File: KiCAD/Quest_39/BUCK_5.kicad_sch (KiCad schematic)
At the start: 21 parts

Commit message: Fixed most ERC errors
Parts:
- gave numbers to parts that had none: 21
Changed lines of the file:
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@@
   (symbol (lib_id "Device:R") (at 60.96 49.53 0) (unit 1)
     (in_bom yes) (on_board yes) (fields_autoplaced)
-    (property "Reference" "R?" (id 0) (at 63.5 48.2599 0)
+    (property "Reference" "R35" (id 0) (at 63.5 48.2599 0)
       (effects (font (size 1.27 1.27)) (justify left))
     )
@@
   (symbol (lib_id "Device:R") (at 48.26 49.53 0) (unit 1)
     (in_bom yes) (on_board yes) (fields_autoplaced)
-    (property "Reference" "R?" (id 0) (at 50.8 48.2599 0)
+    (property "Reference" "R34" (id 0) (at 50.8 48.2599 0)
       (effects (font (size 1.27 1.27)) (justify left))
     )
@@
   (symbol (lib_id "Device:C_Polarized") (at 381 172.72 0) (unit 1)
     (in_bom yes) (on_board yes)
-    (property "Reference" "C?" (id 0) (at 384.7895 171.4075 0)
+    (property "Reference" "C86" (id 0) (at 384.7895 171.4075 0)
       (effects (font (size 1.27 1.27)) (justify left))
     )
@@
   (symbol (lib_id "Device:C_Polarized") (at 393.7 172.72 0) (unit 1)
     (in_bom yes) (on_board yes)
-    (property "Reference" "C?" (id 0) (at 397.4895 171.4075 0)
+    (property "Reference" "C87" (id 0) (at 397.4895 171.4075 0)
       (effects (font (size 1.27 1.27)) (justify left))
     )
@@
   (symbol (lib_id "Device:C_Polarized") (at 86.36 46.99 0) (unit 1)
     (in_bom yes) (on_board yes) (fields_autoplaced)
-    (property "Reference" "C?" (id 0) (at 90.17 44.8309 0)
+    (property "Reference" "C77" (id 0) (at 90.17 44.8309 0)
       (effects (font (size 1.27 1.27)) (justify left))
     )
@@
   (symbol (lib_id "Device:C") (at 125.73 46.99 0) (unit 1)
     (in_bom yes) (on_board yes) (fields_autoplaced)
-    (property "Reference" "C?" (id 0) (at 129.54 45.7199 0)
+    (property "Reference" "C80" (id 0) (at 129.54 45.7199 0)
       (effects (font (size 1.27 1.27)) (justify left))
     )
@@
   (symbol (lib_id "Analog_ADC:INA226") (at 78.74 73.66 0) (unit 1)
     (in_bom yes) (on_board yes)
-    (property "Reference" "U?" (id 0) (at 83.82 62.23 0)
+    (property "Reference" "U25" (id 0) (at 83.82 62.23 0)
       (effects (font (size 1.27 1.27)) (justify left))
     )
@@
   (symbol (lib_id "Device:R") (at 322.58 215.9 0) (unit 1)
     (in_bom yes) (on_board yes) (fields_autoplaced)
-    (property "Reference" "R?" (id 0) (at 325.12 214.6299 0)
+    (property "Reference" "R37" (id 0) (at 325.12 214.6299 0)
       (effects (font (size 1.27 1.27)) (justify left))
     )
@@
   (symbol (lib_id "Device:C") (at 100.33 46.99 0) (unit 1)
     (in_bom yes) (on_board yes) (fields_autoplaced)
-    (property "Reference" "C?" (id 0) (at 104.14 45.7199 0)
+    (property "Reference" "C78" (id 0) (at 104.14 45.7199 0)
       (effects (font (size 1.27 1.27)) (justify left))
     )
@@
   (symbol (lib_id "Amplifier_Operational:MCP601-xOT") (at 35.56 66.04 0) (unit 1)
     (in_bom yes) (on_board yes)
-    (property "Reference" "U?" (id 0) (at 38.1 62.23 0))
+    (property "Reference" "U24" (id 0) (at 38.1 62.23 0))
     (property "Value" "MCP601T-I/OT" (id 1) (at 41.91 69.85 0))
     (property "Footprint" "Package_TO_SOT_SMD:SOT-23-5" (id 2) (at 33.02 71.12 0)
@@
   (symbol (lib_id "MCP4151:MCP4151-502E{slash}SN") (at 254 220.98 0) (unit 1)
     (in_bom yes) (on_board yes)
-    (property "Reference" "U?" (id 0) (at 312.42 214.63 0)
+    (property "Reference" "U27" (id 0) (at 312.42 214.63 0)
       (effects (font (size 1.524 1.524)))
     )
@@
   (symbol (lib_id "Device:C") (at 128.27 137.16 0) (unit 1)
     (in_bom yes) (on_board yes) (fields_autoplaced)
-    (property "Reference" "C?" (id 0) (at 132.08 135.8899 0)
+    (property "Reference" "C82" (id 0) (at 132.08 135.8899 0)
       (effects (font (size 1.27 1.27)) (justify left))
     )
@@
   (symbol (lib_id "Device:C") (at 335.28 172.72 0) (unit 1)
     (in_bom yes) (on_board yes) (fields_autoplaced)
-    (property "Reference" "C?" (id 0) (at 339.09 171.4499 0)
+    (property "Reference" "C83" (id 0) (at 339.09 171.4499 0)
       (effects (font (size 1.27 1.27)) (justify left))
     )
@@
   (symbol (lib_id "LTM4611EV:LTM4611EV-PBF") (at 132.08 102.87 0) (unit 1)
     (in_bom yes) (on_board yes)
-    (property "Reference" "U?" (id 0) (at 308.61 50.8 0)
+    (property "Reference" "U26" (id 0) (at 308.61 50.8 0)
       (effects (font (size 1.524 1.524)))
     )
@@
   (symbol (lib_id "Device:C_Polarized") (at 368.3 172.72 0) (unit 1)
     (in_bom yes) (on_board yes)
-    (property "Reference" "C?" (id 0) (at 372.0895 171.4075 0)
+    (property "Reference" "C85" (id 0) (at 372.0895 171.4075 0)
       (effects (font (size 1.27 1.27)) (justify left))
     )
@@
   (symbol (lib_id "Device:R") (at 127 91.44 0) (unit 1)
     (in_bom yes) (on_board yes) (fields_autoplaced)
-    (property "Reference" "R?" (id 0) (at 129.54 90.1699 0)
+    (property "Reference" "R36" (id 0) (at 129.54 90.1699 0)
       (effects (font (size 1.27 1.27)) (justify left))
     )
@@
   (symbol (lib_id "Device:R") (at 55.88 41.91 90) (unit 1)
     (in_bom yes) (on_board yes) (fields_autoplaced)
-    (property "Reference" "R?" (id 0) (at 55.88 35.56 90))
+    (property "Reference" "R33" (id 0) (at 55.88 35.56 90))
     (property "Value" "0R0025" (id 1) (at 55.88 38.1 90))
     (property "Footprint" "" (id 2) (at 55.88 43.688 90)
@@
   (symbol (lib_id "Device:C") (at 55.88 55.88 90) (unit 1)
     (in_bom yes) (on_board yes)
-    (property "Reference" "C?" (id 0) (at 55.88 52.07 90))
+    (property "Reference" "C81" (id 0) (at 55.88 52.07 90))
     (property "Value" "1uF" (id 1) (at 55.88 59.69 90))
     (property "Footprint" "OptoDevice:R_LDR_4.9x4.2mm_P2.54mm_Vertical" (id 2) (at 59.69 54.9148 0)
@@
   (symbol (lib_id "Device:C") (at 113.03 46.99 0) (unit 1)
     (in_bom yes) (on_board yes) (fields_autoplaced)
-    (property "Reference" "C?" (id 0) (at 116.84 45.7199 0)
+    (property "Reference" "C79" (id 0) (at 116.84 45.7199 0)
       (effects (font (size 1.27 1.27)) (justify left))
     )
@@
   (symbol (lib_id "Device:C_Polarized") (at 354.33 172.72 0) (unit 1)
     (in_bom yes) (on_board yes)
-    (property "Reference" "C?" (id 0) (at 358.1195 171.4075 0)
+    (property "Reference" "C84" (id 0) (at 358.1195 171.4075 0)
       (effects (font (size 1.27 1.27)) (justify left))
     )
@@
   (symbol (lib_id "Device:C") (at 337.82 224.79 0) (unit 1)
     (in_bom yes) (on_board yes) (fields_autoplaced)
-    (property "Reference" "C?" (id 0) (at 341.63 223.5199 0)
-      (effects (font (size 1.27 1.27)) (justify left))
-    )
+    (property "Reference" "C88" (id 0) (at 341.63 223.5199 0)
+      (effects (font (size 1.27 1.27)) (justify left))
+    )

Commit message: Gave all INA226's unique addresses
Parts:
- removed C77: 330uF, symbol Device:C_Polarized
- removed C78, C79, C80: 22uF, symbol Device:C
- removed C81: 1uF, OptoDevice:R_LDR_4.9x4.2mm_P2.54mm_Vertical, symbol Device:C
- removed C82: 100nF, symbol Device:C
- removed C83: 100pF, symbol Device:C
- removed C85, C86, C87: 100uF, symbol Device:C_Polarized
- removed R33: 0R0025, symbol Device:R
- removed R34, R35: 10, symbol Device:R
- removed R36: 10K, symbol Device:R
- removed R37: 20K, symbol Device:R
- removed U24: MCP601T-I/OT, Package_TO_SOT_SMD:SOT-23-5, symbol Amplifier_Operational:MCP601-xOT
- added C85, C86, C87: 22uF, symbol Device:C
- added C89, C90, C97: 100nF, symbol Device:C
- added C91: 10nF, symbol Device:C
- added C92, C93, C94, C95: 100uF, symbol Device:C_Polarized
- added C96: 100pF, symbol Device:C
- added R52: 0R0025, symbol Device:R
- added R53, R54: 10R, symbol Device:R
- added R55: 9k, symbol Device:R
- added R56: 1k, symbol Device:R
- added R57: 10k, symbol Device:R
- added R58: 20K, symbol Device:R
- added TP41, TP42, TP43, TP44, TP45, TP46, TP47: TestPoint, symbol Connector:TestPoint
- added U24: AD626ANZ, N_8_ADI, symbol AD626ANZ:AD626ANZ
- C84: value 100uF -> 330uF
- C88: value 100nF -> 1uF; footprint (none) -> OptoDevice:R_LDR_4.9x4.2mm_P2.54mm_Vertical
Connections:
- net +5V: now also U25.1 (A1), U25.2 (A0), C90.1, C97.1, U24.6 (+VS); no longer C88.1
- net GND: now also C89.2, C90.2, C97.2, U24.2 (AGND), U24.3 (-VS); no longer C88.2, U25.1 (A1), U25.2 (A0), U25.3 (~{Alert})
- net NEG: now also C85.2, C86.2, C87.2, C91.1, C92.2, C93.2, C94.2, C95.2, R56.2, U24.1 (-IN); no longer U25.8 (Vbus)
- net P0A: now also R58.2
- net POS: now also C92.1, C93.1, C94.1, C95.1, C96.1; no longer C84.1
- net PV_POS: now also C84.1, U26.A1 (VIN), U26.A2 (VIN), U26.A3 (VIN), U26.A4 (VIN), U26.A5 (VIN), U26.A6 (VIN), U26.B1 (VIN), U26.B2 (VIN), U26.B3 (VIN), U26.B4 (VIN), U26.B5 (VIN), U26.B6 (VIN), U26.C1 (VIN), U26.C2 (VIN), U26.C3 (VIN), U26.C4 (VIN), U26.C5 (VIN), U26.C6 (VIN), C85.1, C86.1, C87.1, R52.1, R52.2, R53.1, R54.1, R55.1, R57.1
- net RUN: now also R57.2
- net TRACK/SS: now also C91.2
- net Vfb: now also C96.2, R58.1
- net Vin+: now also C88.1, R53.2
- net Vin-: now also C88.2, U25.8 (Vbus), U25.9 (Vin-), R54.2, TP42.1, U24.5 (OUT)
- net at U26.A11 (COMP): now also TP45.1
- net at U26.A7 (INTVCC): now also U26.D9 (INTVCC), TP41.1
- net at U26.B12 (PLLFLTR/FSET): now also TP44.1
- net at U26.F11 (PGOOD): now also U26.G12 (PGOOD), TP43.1
- net at U26.K12 (DIFFVOUT), U26.L12 (VOUT_LCL): now also TP46.1, TP47.1
- new net: C89.1, U24.4 (FILTER)
- new net +IN: R55.2, R56.1, U24.8 (+IN)
- no-connect marks 16 -> 12
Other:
- note added: "10:1 divider"
- note added: "Addr=0x45"
- note added: "Extra mounting"
- note added: "G=10"
- note added: "Output voltage is set by varying Rfb with a digipot. SPI = 00"
- note added: "the measured voltage is divided and then amplified by 10 as to simulate a follower. This is done to make use of the AD626 (low price and availability)."

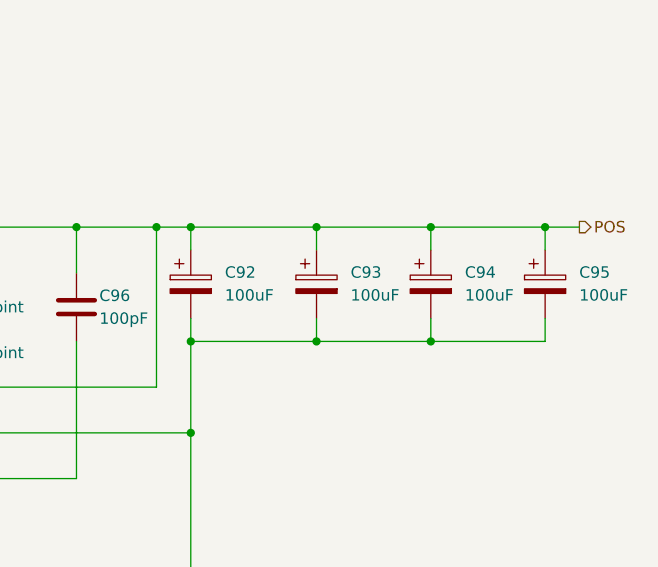
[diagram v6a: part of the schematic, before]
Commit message: Assigned all schem. symbols their footprints
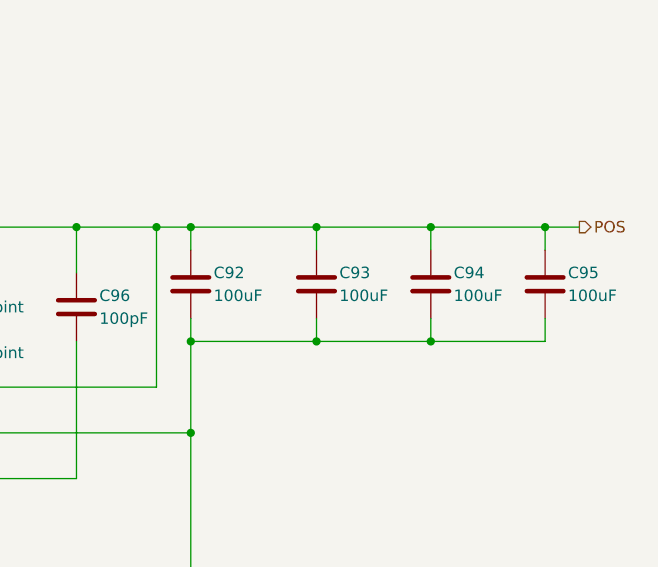
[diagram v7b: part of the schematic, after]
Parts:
- removed C92, C93, C94, C95: 100uF, symbol Device:C_Polarized
- added C92, C93, C94, C95: 100uF, Capacitor_SMD:C_1206_3216Metric, symbol Device:C
- C84: footprint (none) -> Capacitor_SMD:CP_Elec_8x6.9
- C85, C86, C87, C89, C90, C91, C96, C97: footprint (none) -> Capacitor_SMD:C_0805_2012Metric
- C88: footprint OptoDevice:R_LDR_4.9x4.2mm_P2.54mm_Vertical -> Capacitor_SMD:C_0805_2012Metric
- R52: footprint (none) -> Resistor_SMD:R_1206_3216Metric
- R53, R54, R55, R56, R57, R58: footprint (none) -> Resistor_SMD:R_0805_2012Metric
- TP41, TP42, TP43, TP44, TP45, TP46, TP47: footprint (none) -> TestPoint:TestPoint_Pad_D2.0mm
- U24: footprint N_8_ADI -> Package_DIP:DIP-8_W7.62mm_Socket_LongPads
- U26: footprint LGA-133_3_LIT -> Package_LGA:Linear_LGA-133_15.0x15.0mm_Layout12x12_P1.27mm
- U27: footprint SOIC8-N_MC_MCH -> Package_SO:MSOP-8_3x3mm_P0.65mm
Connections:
- net NEG: now also C92.2, C93.2, C94.2, C95.2
- net POS: now also C92.1, C93.1, C94.1, C95.1

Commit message: Initial work on layout
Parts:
- C88, C89, C90, C91, C96, C97: footprint Capacitor_SMD:C_0805_2012Metric -> Capacitor_SMD:C_0603_1608Metric
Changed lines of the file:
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@@
       (effects (font (size 1.27 1.27)) (justify left))
     )
-    (property "Footprint" "Capacitor_SMD:C_0805_2012Metric" (id 2) (at 26.3652 82.55 0)
+    (property "Footprint" "Capacitor_SMD:C_0603_1608Metric" (id 2) (at 26.3652 82.55 0)
       (effects (font (size 1.27 1.27)) hide)
     )
@@
       (effects (font (size 1.27 1.27)) (justify left))
     )
-    (property "Footprint" "Capacitor_SMD:C_0805_2012Metric" (id 2) (at 64.4652 83.82 0)
+    (property "Footprint" "Capacitor_SMD:C_0603_1608Metric" (id 2) (at 64.4652 83.82 0)
       (effects (font (size 1.27 1.27)) hide)
     )
@@
     (property "Reference" "C88" (id 0) (at 74.93 58.42 90))
     (property "Value" "1uF" (id 1) (at 74.93 66.04 90))
-    (property "Footprint" "Capacitor_SMD:C_0805_2012Metric" (id 2) (at 78.74 61.2648 0)
+    (property "Footprint" "Capacitor_SMD:C_0603_1608Metric" (id 2) (at 78.74 61.2648 0)
       (effects (font (size 1.27 1.27)) hide)
     )
@@
       (effects (font (size 1.27 1.27)) (justify left))
     )
-    (property "Footprint" "Capacitor_SMD:C_0805_2012Metric" (id 2) (at 341.3252 222.25 0)
+    (property "Footprint" "Capacitor_SMD:C_0603_1608Metric" (id 2) (at 341.3252 222.25 0)
       (effects (font (size 1.27 1.27)) hide)
     )
@@
       (effects (font (size 1.27 1.27)) (justify left))
     )
-    (property "Footprint" "Capacitor_SMD:C_0805_2012Metric" (id 2) (at 345.1352 170.18 0)
+    (property "Footprint" "Capacitor_SMD:C_0603_1608Metric" (id 2) (at 345.1352 170.18 0)
       (effects (font (size 1.27 1.27)) hide)
     )
@@
       (effects (font (size 1.27 1.27)) (justify left))
     )
-    (property "Footprint" "Capacitor_SMD:C_0805_2012Metric" (id 2) (at 106.3752 125.73 0)
-      (effects (font (size 1.27 1.27)) hide)
-    )
+    (property "Footprint" "Capacitor_SMD:C_0603_1608Metric" (id 2) (at 106.3752 125.73 0)
+      (effects (font (size 1.27 1.27)) hide)
+    )
